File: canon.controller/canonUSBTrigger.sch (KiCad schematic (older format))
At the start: 20 parts, among them IC1 MCP2200, J1 USB112A, K1 CONN_3, P1 CONN_2, P2 CONN_2, P3 CONN_2, U1 RESONATOR, U2 OPTO-TRANSISTOR, U3 OPTO-TRANSISTOR

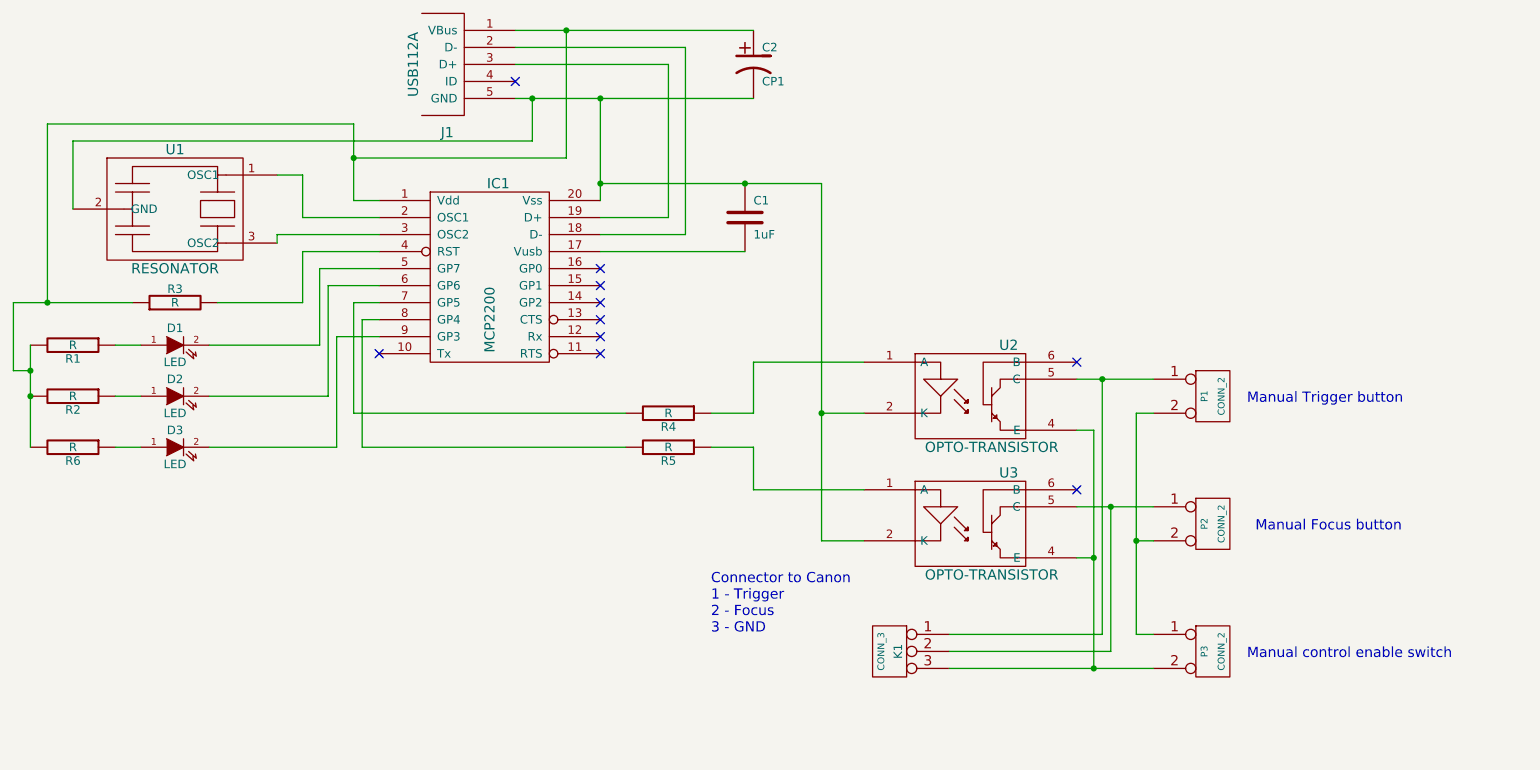
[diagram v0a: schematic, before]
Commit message: canon trigger updated
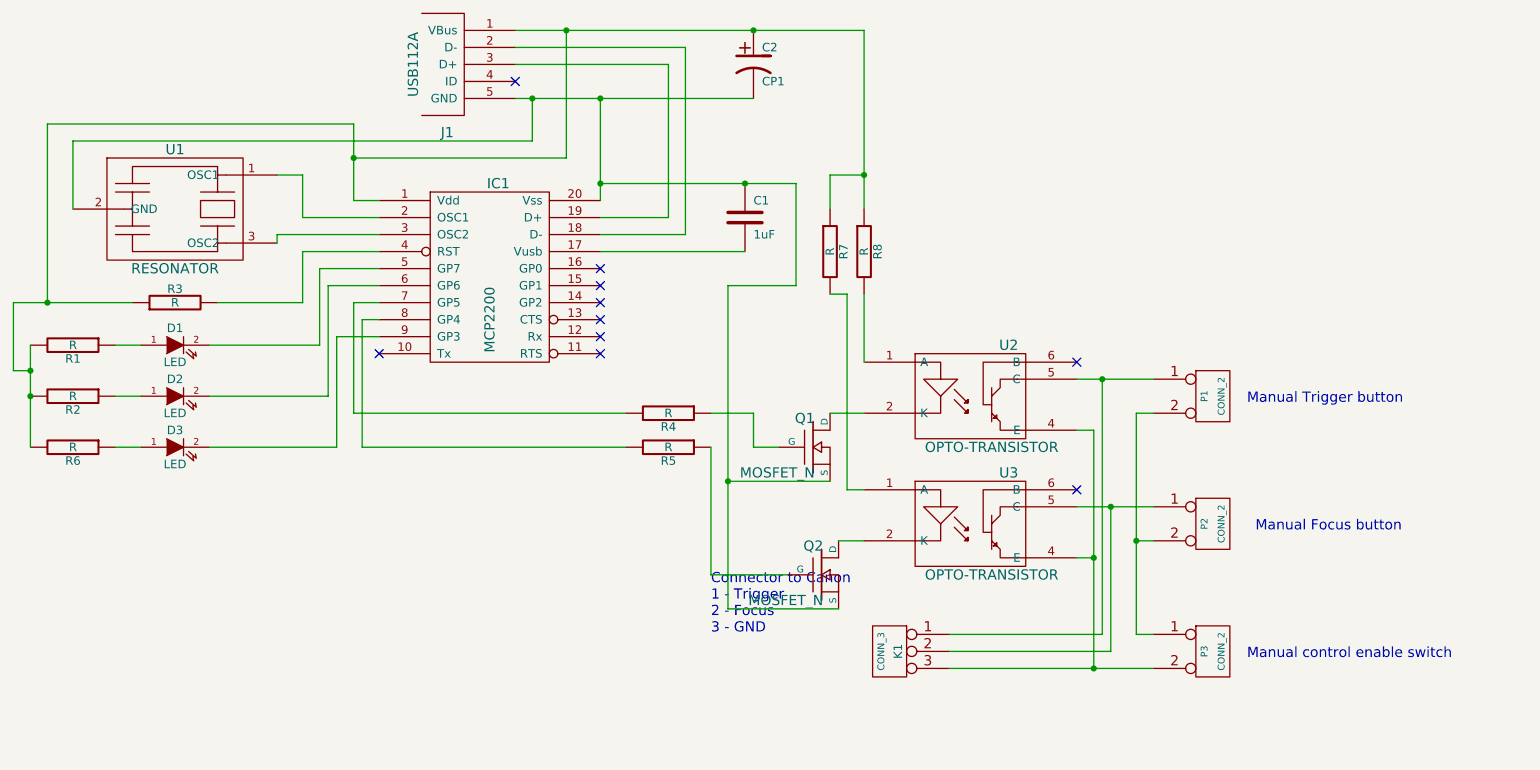
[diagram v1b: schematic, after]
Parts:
- added Q1, Q2: MOSFET_N, symbol MOSFET_N
- added R7, R8: R, symbol R
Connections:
- net at C2.1, IC1.1 (Vdd), J1.1 (VBus)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: now also R7.1, R8.1
- net at C1.1, C2.2, IC1.20 (Vss)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: now also Q1.S, Q2.S; no longer U2.2 (K), U3.2 (K)
- net at U2.1 (A): now also R8.2; no longer R4.1
- net at U3.1 (A): now also R7.2; no longer R5.1
- new net: Q1.D, U2.2 (K)
- new net: Q2.D, U3.2 (K)
- new net: Q1.G, R4.1
- new net: Q2.G, R5.1
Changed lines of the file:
@@
-EESchema Schematic File Version 2  date 2012. 09. 06. 11:12:06
+EESchema Schematic File Version 2  date Sat 22 Sep 2012 16:52:20 CEST
 LIBS:resonator
 LIBS:usb112a
@@
 LIBS:contrib
 LIBS:valves
-EELAYER 43  0
+LIBS:canonUSBTrigger-cache
+EELAYER 25  0
 EELAYER END
-$Descr A4 11700 8267
+$Descr A4 11693 8268
 encoding utf-8
 Sheet 1 1
 Title ""
-Date "6 sep 2012"
+Date "22 sep 2012"
 Rev ""
 Comp ""
@@
 NoConn ~ 5150 3850
 NoConn ~ 3850 3850
-Connection ~ 1800 4100
-Wire Wire Line
-	1800 4400 1800 3800
-Wire Wire Line
-	3850 3750 3600 3750
-Wire Wire Line
-	3600 3750 3600 4400
-Wire Wire Line
-	3600 4400 2850 4400
-Connection ~ 6000 2850
-Wire Wire Line
-	6700 4950 6450 4950
-Wire Wire Line
-	6450 4950 6450 2850
-Wire Wire Line
-	6450 2850 5150 2850
-Wire Wire Line
-	6700 3900 6050 3900
-Wire Wire Line
-	6050 3900 6050 4200
-Wire Wire Line
-	6050 4200 5800 4200
-Wire Wire Line
-	4650 1950 6050 1950
-Wire Wire Line
-	8400 4200 8300 4200
-Wire Wire Line
-	8300 4200 8300 5500
-Wire Wire Line
-	8300 5500 8400 5500
-Connection ~ 8050 5050
-Wire Wire Line
-	7950 5050 8050 5050
-Connection ~ 8150 4750
-Wire Wire Line
-	8150 4750 8150 5600
-Wire Wire Line
-	8150 5600 7200 5600
-Wire Wire Line
-	8400 4750 7950 4750
-Wire Wire Line
-	5300 4400 3750 4400
-Wire Wire Line
-	3750 4400 3750 3650
-Wire Wire Line
-	3750 3650 3850 3650
-Connection ~ 1900 3550
-Wire Wire Line
-	2400 3550 1700 3550
-Wire Wire Line
-	1700 3550 1700 3950
-Connection ~ 1800 3950
-Wire Wire Line
-	1700 3950 1800 3950
-Wire Wire Line
-	2300 4100 2450 4100
-Wire Wire Line
-	2850 4100 3550 4100
-Wire Wire Line
-	3550 4100 3550 3450
-Wire Wire Line
-	3550 3450 3850 3450
-Connection ~ 3700 2700
-Wire Wire Line
-	3700 2500 3700 2950
-Wire Wire Line
-	3700 2500 1900 2500
-Wire Wire Line
-	1900 2500 1900 3550
-Connection ~ 5150 2350
-Connection ~ 5150 2850
-Connection ~ 4750 2350
-Wire Wire Line
-	4750 2350 4750 2600
-Wire Wire Line
-	4750 2600 2050 2600
-Wire Wire Line
-	2050 2600 2050 3000
-Wire Wire Line
-	3850 3050 3400 3050
-Wire Wire Line
-	3400 3050 3400 2800
-Wire Wire Line
-	3400 2800 3250 2800
-Wire Wire Line
-	3700 2950 3850 2950
-Wire Wire Line
-	3700 2700 4950 2700
-Wire Wire Line
-	4950 2700 4950 1950
-Wire Wire Line
-	5150 3050 5550 3050
-Wire Wire Line
-	5550 3050 5550 2150
-Wire Wire Line
-	5550 2150 4650 2150
-Wire Wire Line
-	4650 2050 5650 2050
-Wire Wire Line
-	5650 2050 5650 3150
-Wire Wire Line
-	5650 3150 5150 3150
-Wire Wire Line
-	5150 2950 5150 2350
-Wire Wire Line
-	3850 3150 3250 3150
-Wire Wire Line
-	3250 3150 3250 3200
-Wire Wire Line
-	5150 3250 6000 3250
-Connection ~ 4950 1950
-Wire Wire Line
-	2900 3550 3400 3550
-Wire Wire Line
-	3400 3550 3400 3250
-Wire Wire Line
-	3400 3250 3850 3250
-Wire Wire Line
-	2850 3800 3500 3800
-Wire Wire Line
-	3500 3800 3500 3350
-Wire Wire Line
-	3500 3350 3850 3350
-Wire Wire Line
-	2450 3800 2300 3800
-Wire Wire Line
-	5300 4200 3700 4200
-Wire Wire Line
-	3700 4200 3700 3550
-Wire Wire Line
-	3700 3550 3850 3550
-Wire Wire Line
-	6050 2350 4650 2350
-Wire Wire Line
-	8400 4000 7950 4000
-Wire Wire Line
-	7200 5500 8100 5500
-Wire Wire Line
-	8100 5500 8100 4000
-Connection ~ 8100 4000
-Wire Wire Line
-	7950 4300 8050 4300
-Wire Wire Line
-	8050 4300 8050 5700
-Wire Wire Line
-	7200 5700 8400 5700
-Connection ~ 8050 5700
-Wire Wire Line
-	8400 4950 8300 4950
-Connection ~ 8300 4950
-Wire Wire Line
-	5800 4400 6050 4400
-Wire Wire Line
-	6050 4400 6050 4650
-Wire Wire Line
-	6050 4650 6700 4650
-Wire Wire Line
-	6700 4200 6450 4200
-Connection ~ 6450 4200
-Wire Wire Line
-	2450 4400 2300 4400
 $Comp
 L R R6
@@
 	1    0    0    -1
 $EndComp
+$Comp
+L MOSFET_N Q2
+U 1 1 505DC738
+P 6450 5150
+F 0 "Q2" H 6460 5320 60  0000 R CNN
+F 1 "MOSFET_N" H 6460 5000 60  0000 R CNN
+	1    6450 5150
+	1    0    0    -1
+$EndComp
+$Comp
+L MOSFET_N Q1
+U 1 1 505DC747
+P 6400 4400
+F 0 "Q1" H 6410 4570 60  0000 R CNN
+F 1 "MOSFET_N" H 6410 4250 60  0000 R CNN
+	1    6400 4400
+	1    0    0    -1
+$EndComp
+$Comp
+L R R8
+U 1 1 505DC757
+P 6700 3250
+F 0 "R8" V 6780 3250 50  0000 C CNN
+F 1 "R" V 6700 3250 50  0000 C CNN
+	1    6700 3250
+	1    0    0    -1
+$EndComp
+$Comp
+L R R7
+U 1 1 505DC766
+P 6500 3250
+F 0 "R7" V 6580 3250 50  0000 C CNN
+F 1 "R" V 6500 3250 50  0000 C CNN
+	1    6500 3250
+	1    0    0    -1
+$EndComp
+Connection ~ 1800 4100
+Wire Wire Line
+	1800 3800 1800 4400
+Wire Wire Line
+	3850 3750 3600 3750
+Wire Wire Line
+	3600 3750 3600 4400
+Wire Wire Line
+	3600 4400 2850 4400
+Wire Wire Line
+	5150 2850 6300 2850
+Wire Wire Line
+	4650 1950 6700 1950
+Wire Wire Line
+	8400 4200 8300 4200
+Wire Wire Line
+	8300 4200 8300 5500
+Wire Wire Line
+	8300 5500 8400 5500
+Connection ~ 8050 5050
+Wire Wire Line
+	7950 5050 8050 5050
+Connection ~ 8150 4750
+Wire Wire Line
+	8150 4750 8150 5600
+Wire Wire Line
+	8150 5600 7200 5600
+Wire Wire Line
+	7950 4750 8400 4750
+Wire Wire Line
+	5300 4400 3750 4400
+Wire Wire Line
+	3750 4400 3750 3650
+Wire Wire Line
+	3750 3650 3850 3650
+Connection ~ 1900 3550
+Wire Wire Line
+	1700 3550 2400 3550
+Wire Wire Line
+	1700 3550 1700 3950
+Connection ~ 1800 3950
+Wire Wire Line
+	1700 3950 1800 3950
+Wire Wire Line
+	2300 4100 2450 4100
+Wire Wire Line
+	2850 4100 3550 4100
+Wire Wire Line
+	3550 4100 3550 3450
+Wire Wire Line
+	3550 3450 3850 3450
+Connection ~ 3700 2700
+Wire Wire Line
+	3700 2500 3700 2950
+Wire Wire Line
+	3700 2500 1900 2500
+Wire Wire Line
+	1900 2500 1900 3550
+Connection ~ 5150 2350
+Connection ~ 5150 2850
+Connection ~ 4750 2350
+Wire Wire Line
+	4750 2350 4750 2600
+Wire Wire Line
+	4750 2600 2050 2600
+Wire Wire Line
+	2050 2600 2050 3000
+Wire Wire Line
+	3850 3050 3400 3050
+Wire Wire Line
+	3400 3050 3400 2800
+Wire Wire Line
+	3400 2800 3250 2800
+Wire Wire Line
+	3700 2950 3850 2950
+Wire Wire Line
+	3700 2700 4950 2700
+Wire Wire Line
+	4950 2700 4950 1950
+Wire Wire Line
+	5150 3050 5550 3050
+Wire Wire Line
+	5550 3050 5550 2150
+Wire Wire Line
+	5550 2150 4650 2150
+Wire Wire Line
+	4650 2050 5650 2050
+Wire Wire Line
+	5650 2050 5650 3150
+Wire Wire Line
+	5650 3150 5150 3150
+Wire Wire Line
+	5150 2350 5150 2950
+Wire Wire Line
+	3850 3150 3250 3150
+Wire Wire Line
+	3250 3150 3250 3200
+Wire Wire Line
+	5150 3250 6000 3250
+Connection ~ 4950 1950
+Wire Wire Line
+	2900 3550 3400 3550
+Wire Wire Line
+	3400 3550 3400 3250
+Wire Wire Line
+	3400 3250 3850 3250
+Wire Wire Line
+	2850 3800 3500 3800
+Wire Wire Line
+	3500 3800 3500 3350
+Wire Wire Line
+	3500 3350 3850 3350
+Wire Wire Line
+	2450 3800 2300 3800
+Wire Wire Line
+	5300 4200 3700 4200
+Wire Wire Line
+	3700 4200 3700 3550
+Wire Wire Line
+	3700 3550 3850 3550
+Wire Wire Line
+	4650 2350 6050 2350
+Wire Wire Line
+	7950 4000 8400 4000
+Wire Wire Line
+	7200 5500 8100 5500
+Wire Wire Line
+	8100 5500 8100 4000
+Connection ~ 8100 4000
+Wire Wire Line
+	7950 4300 8050 4300
+Wire Wire Line
+	8050 4300 8050 5700
+Wire Wire Line
+	7200 5700 8400 5700
+Connection ~ 8050 5700
+Wire Wire Line
+	8400 4950 8300 4950
+Connection ~ 8300 4950
+Wire Wire Line
+	2450 4400 2300 4400
+Wire Wire Line
+	6700 1950 6700 3000
+Connection ~ 6050 1950
+Wire Wire Line
+	6500 3000 6500 2800
+Wire Wire Line
+	6500 2800 6700 2800
+Connection ~ 6700 2800
+Wire Wire Line
+	6700 3500 6700 3900
+Wire Wire Line
+	6700 4650 6600 4650
+Wire Wire Line
+	6600 4650 6600 3500
+Wire Wire Line
+	6600 3500 6500 3500
+Wire Wire Line
+	6700 4200 6500 4200
+Wire Wire Line
+	6700 4950 6550 4950
+Wire Wire Line
+	5900 5350 6550 5350
+Wire Wire Line
+	5900 3450 5900 5350
+Wire Wire Line
+	5900 3450 6300 3450
+Wire Wire Line
+	6300 3450 6300 2850
+Connection ~ 6000 2850
+Wire Wire Line
+	5800 4400 5800 5150
+Wire Wire Line
+	5800 5150 6250 5150
+Wire Wire Line
+	6500 4600 5900 4600
+Connection ~ 5900 4600
+Wire Wire Line
+	6200 4400 6050 4400
+Wire Wire Line
+	6050 4400 6050 4200
+Wire Wire Line
+	6050 4200 5800 4200
 $EndSCHEMATC

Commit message: Cannon USB trigger PSB design exported to gerber format. Ready to be printed
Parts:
- added JP1: JUMPER3, symbol JUMPER3
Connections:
- net at U2.4 (E), U3.4 (E): no longer K1.3 (P3), P3.2 (PM)
- net at K1.2 (PM), P2.1 (P1), U3.5 (C): now also JP1.2
- net at P1.2 (PM), P2.2 (PM), P3.1 (P1): now also JP1.3
- new net: JP1.1, K1.3 (P3), P3.2 (PM)
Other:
- note added: "Is the USB trigger can be disabled by the switch"
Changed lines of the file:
@@
-EESchema Schematic File Version 2  date Sat 22 Sep 2012 16:52:20 CEST
+EESchema Schematic File Version 2  date Sun 23 Sep 2012 13:07:19 CEST
 LIBS:resonator
 LIBS:usb112a
@@
 Sheet 1 1
 Title ""
-Date "22 sep 2012"
+Date "23 sep 2012"
 Rev ""
 Comp ""
@@
 	1    0    0    -1
 $EndComp
+$Comp
+L JUMPER3 JP1
+U 1 1 505EEC90
+P 8050 5900
+F 0 "JP1" H 8100 5800 40  0000 L CNN
+F 1 "JUMPER3" H 8050 6000 40  0000 C CNN
+	1    8050 5900
+	1    0    0    -1
+$EndComp
 Connection ~ 1800 4100
 Wire Wire Line
@@
 	8400 4200 8300 4200
 Wire Wire Line
-	8300 4200 8300 5500
+	8300 4200 8300 5900
 Wire Wire Line
 	8300 5500 8400 5500
-Connection ~ 8050 5050
 Wire Wire Line
 	7950 5050 8050 5050
@@
 	7950 4300 8050 4300
 Wire Wire Line
-	8050 4300 8050 5700
+	8050 4300 8050 5050
 Wire Wire Line
 	7200 5700 8400 5700
-Connection ~ 8050 5700
 Wire Wire Line
 	8400 4950 8300 4950
@@
 Wire Wire Line
 	6050 4200 5800 4200
+Wire Wire Line
+	7600 5700 7600 5900
+Wire Wire Line
+	7600 5900 7800 5900
+Connection ~ 7600 5700
+Connection ~ 8300 5500
+Connection ~ 8300 5500
+Wire Wire Line
+	7700 5600 7700 6100
+Wire Wire Line
+	7700 6100 8050 6100
+Wire Wire Line
+	8050 6100 8050 6000
+Connection ~ 7700 5600
+Text Notes 7300 6200 0    60   ~ 0
+Is the USB trigger can be disabled by the switch
 $EndSCHEMATC
